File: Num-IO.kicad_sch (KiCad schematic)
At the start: 27 parts, among them J5 Conn_01x02_Male, J6 Conn_01x02_Male, J7 Conn_01x02_Male, U3 MAX14851AEE+

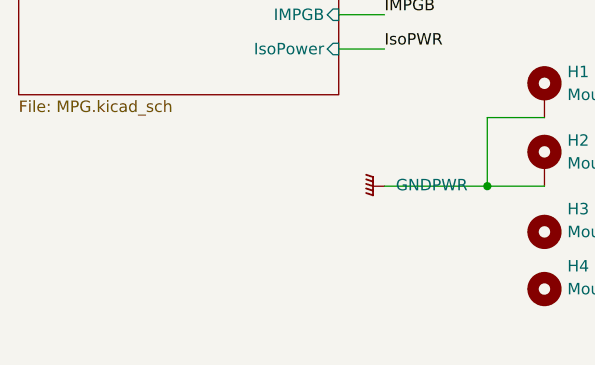
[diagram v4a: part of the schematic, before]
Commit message: add mounting holes for stencil (not sure if correct) + specify where to put prod number ("JLCJLCJLCJLC")
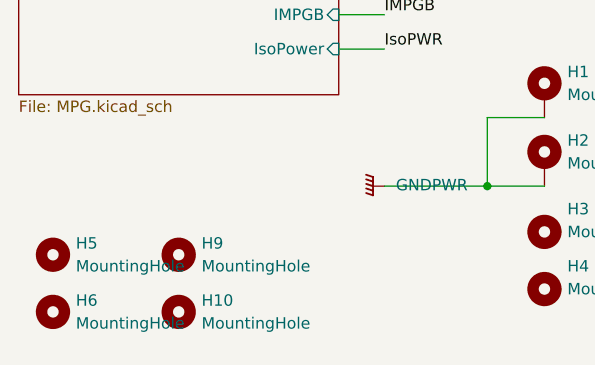
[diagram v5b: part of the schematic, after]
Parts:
- added H10, H9: MountingHole, MountingHole:MountingHole_5mm, symbol Mechanical:MountingHole
- added H5, H6: MountingHole, MountingHole:MountingHole_3mm, symbol Mechanical:MountingHole
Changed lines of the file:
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@@
     (pin "1")
+  )
+  (symbol (lib_id "Mechanical:MountingHole") (at 20.32 191.77 0) (unit 1)
+    (in_bom yes) (on_board yes) (fields_autoplaced)
+    (property "Reference" "H6" (id 0) (at 22.86 190.4999 0)
+      (effects (font (size 1.27 1.27)) (justify left))
+    )
+    (property "Value" "MountingHole" (id 1) (at 22.86 193.0399 0)
+      (effects (font (size 1.27 1.27)) (justify left))
+    )
+    (property "Footprint" "MountingHole:MountingHole_3mm" (id 2) (at 20.32 191.77 0)
+      (effects (font (size 1.27 1.27)) hide)
+    )
+    (property "Datasheet" "~" (id 3) (at 20.32 191.77 0)
+      (effects (font (size 1.27 1.27)) hide)
+    )
   )
   (symbol (lib_id "Mechanical:MountingHole") (at 74.93 189.23 0) (unit 1)
@@
     (pin "1")
   )
+  (symbol (lib_id "Mechanical:MountingHole") (at 20.32 185.42 0) (unit 1)
+    (in_bom yes) (on_board yes) (fields_autoplaced)
+    (property "Reference" "H5" (id 0) (at 22.86 184.1499 0)
+      (effects (font (size 1.27 1.27)) (justify left))
+    )
+    (property "Value" "MountingHole" (id 1) (at 22.86 186.6899 0)
+      (effects (font (size 1.27 1.27)) (justify left))
+    )
+    (property "Footprint" "MountingHole:MountingHole_3mm" (id 2) (at 20.32 185.42 0)
+      (effects (font (size 1.27 1.27)) hide)
+    )
+    (property "Datasheet" "~" (id 3) (at 20.32 185.42 0)
+      (effects (font (size 1.27 1.27)) hide)
+    )
+  )
   (symbol (lib_id "Diode:SM6T36A") (at 124.46 120.65 0) (mirror y) (unit 1)
     (in_bom yes) (on_board yes) (fields_autoplaced)
@@
     (pin "2")
   )
+  (symbol (lib_id "Mechanical:MountingHole") (at 34.29 191.77 0) (unit 1)
+    (in_bom yes) (on_board yes) (fields_autoplaced)
+    (property "Reference" "H10" (id 0) (at 36.83 190.4999 0)
+      (effects (font (size 1.27 1.27)) (justify left))
+    )
+    (property "Value" "MountingHole" (id 1) (at 36.83 193.0399 0)
+      (effects (font (size 1.27 1.27)) (justify left))
+    )
+    (property "Footprint" "MountingHole:MountingHole_5mm" (id 2) (at 34.29 191.77 0)
+      (effects (font (size 1.27 1.27)) hide)
+    )
+    (property "Datasheet" "~" (id 3) (at 34.29 191.77 0)
+      (effects (font (size 1.27 1.27)) hide)
+    )
+  )
   (symbol (lib_id "Device:R") (at 149.86 123.19 90) (unit 1)
     (in_bom yes) (on_board yes) (fields_autoplaced)
@@
     (pin "1")
     (pin "2")
+  )
+  (symbol (lib_id "Mechanical:MountingHole") (at 34.29 185.42 0) (unit 1)
+    (in_bom yes) (on_board yes) (fields_autoplaced)
+    (property "Reference" "H9" (id 0) (at 36.83 184.1499 0)
+      (effects (font (size 1.27 1.27)) (justify left))
+    )
+    (property "Value" "MountingHole" (id 1) (at 36.83 186.6899 0)
+      (effects (font (size 1.27 1.27)) (justify left))
+    )
+    (property "Footprint" "MountingHole:MountingHole_5mm" (id 2) (at 34.29 185.42 0)
+      (effects (font (size 1.27 1.27)) hide)
+    )
+    (property "Datasheet" "~" (id 3) (at 34.29 185.42 0)
+      (effects (font (size 1.27 1.27)) hide)
+    )
   )
   (symbol (lib_id "Diode:SM6T36A") (at 124.46 115.57 0) (mirror y) (unit 1)
@@
       (reference "H4") (unit 1) (value "MountingHole_Pad") (footprint "MountingHole:MountingHole_3.2mm_M3_DIN965_Pad")
     )
+    (path "/8a465242-5cdc-4617-8be3-010332d89589"
+      (reference "H5") (unit 1) (value "MountingHole") (footprint "MountingHole:MountingHole_3mm")
+    )
+    (path "/0ef4566a-f178-40cc-a5e3-c7d5f850c862"
+      (reference "H6") (unit 1) (value "MountingHole") (footprint "MountingHole:MountingHole_3mm")
+    )
+    (path "/9b2243e1-b4a5-4d8d-b925-203eb710e075"
+      (reference "H9") (unit 1) (value "MountingHole") (footprint "MountingHole:MountingHole_5mm")
+    )
+    (path "/90d47418-a546-4a60-a25f-b66a00e8b651"
+      (reference "H10") (unit 1) (value "MountingHole") (footprint "MountingHole:MountingHole_5mm")
+    )
     (path "/f406686c-9281-4d3d-803f-df6f4de4bd3f/eb79cea9-fa97-475b-90d4-17b2843503f4"

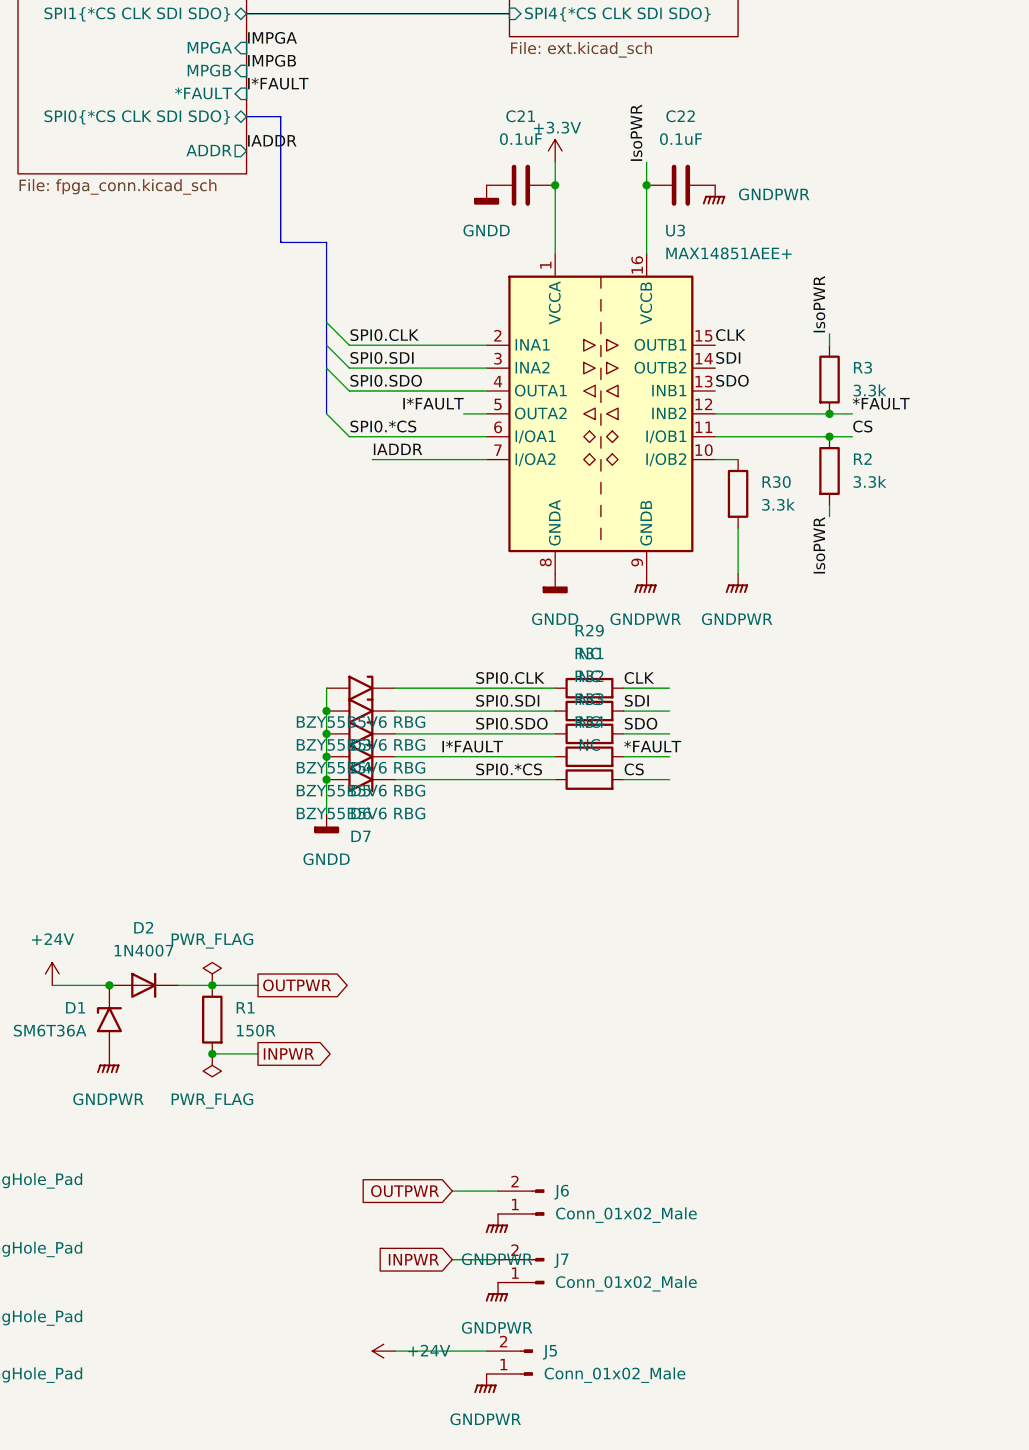
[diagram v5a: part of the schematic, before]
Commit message: fixes after V1
4 resistors for input power
disable CRCEN
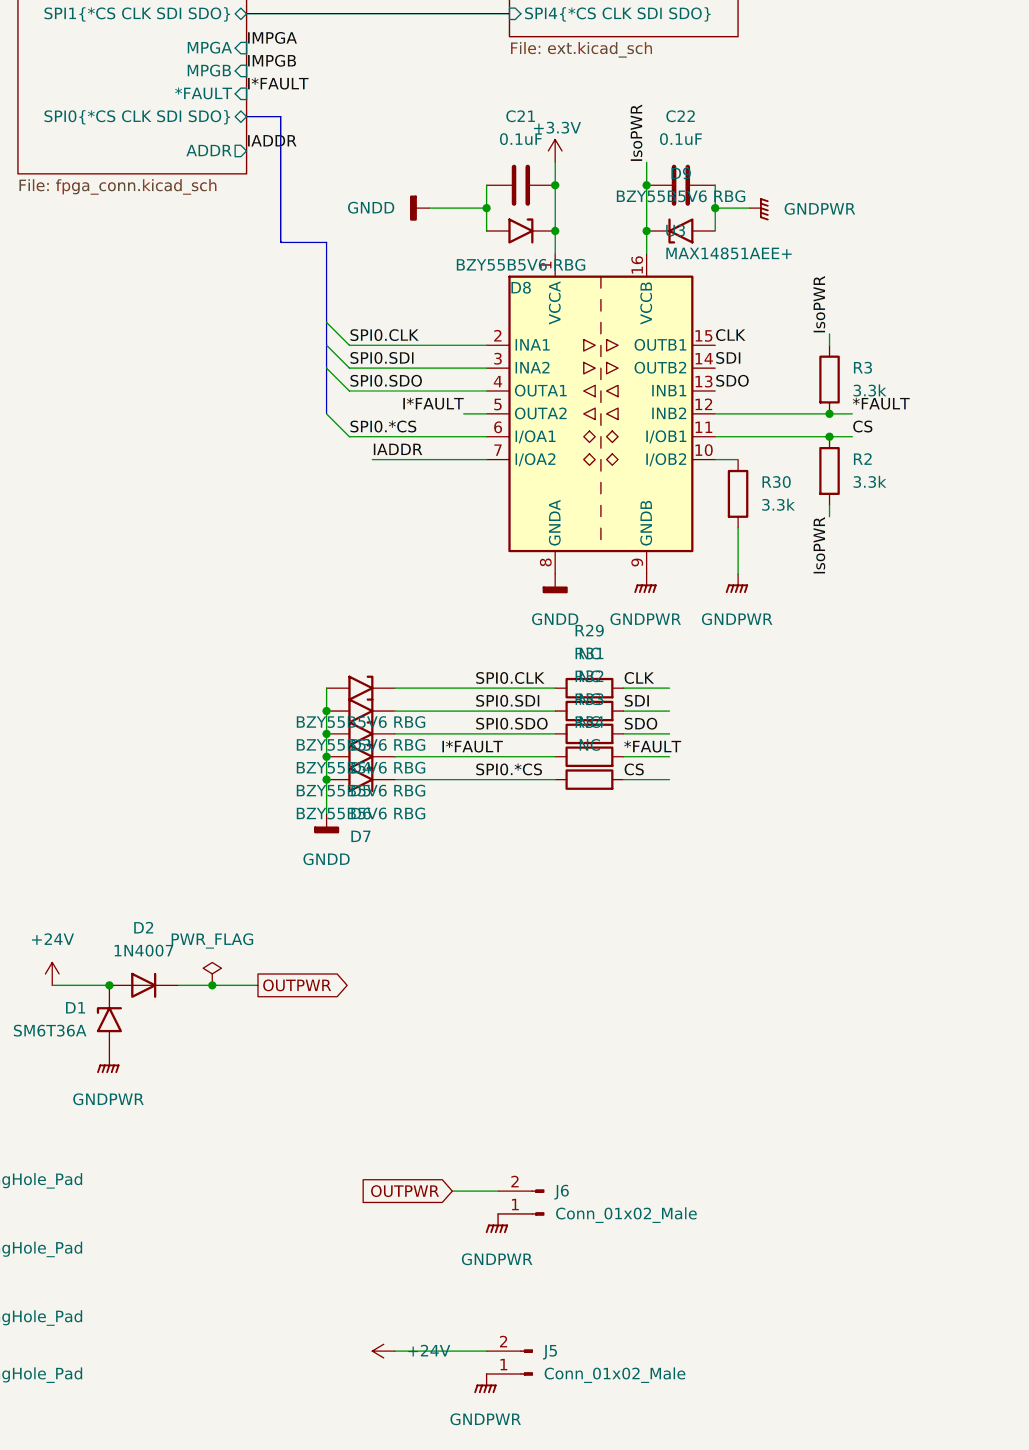
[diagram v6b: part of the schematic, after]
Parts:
- removed J7: Conn_01x02_Male, Connector_Molex:Molex_KK-254_AE-6410-02A_1x02_P2.54mm_Vertical, symbol Connector:Conn_01x02_Male
- removed R1: 150R, Resistor_SMD:R_0805_2012Metric, symbol Device:R
- added D8, D9: BZY55B5V6 RBG, Diode_SMD:D_0805_2012Metric, symbol Diode:SM6T36A
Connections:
- net +3V3: now also D8.1 (A1)
- net GNDD: now also D8.2 (A2)
- net GNDPWR: now also D9.2 (A2)
- net IsoPWR: now also D9.1 (A1)
